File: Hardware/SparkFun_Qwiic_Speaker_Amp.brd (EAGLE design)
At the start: 43.2 x 25.4 mm, 93 parts, among them J1 QWIIC, J2 TRS_INPUT, J6 SCREW, U6 TPA2016D2

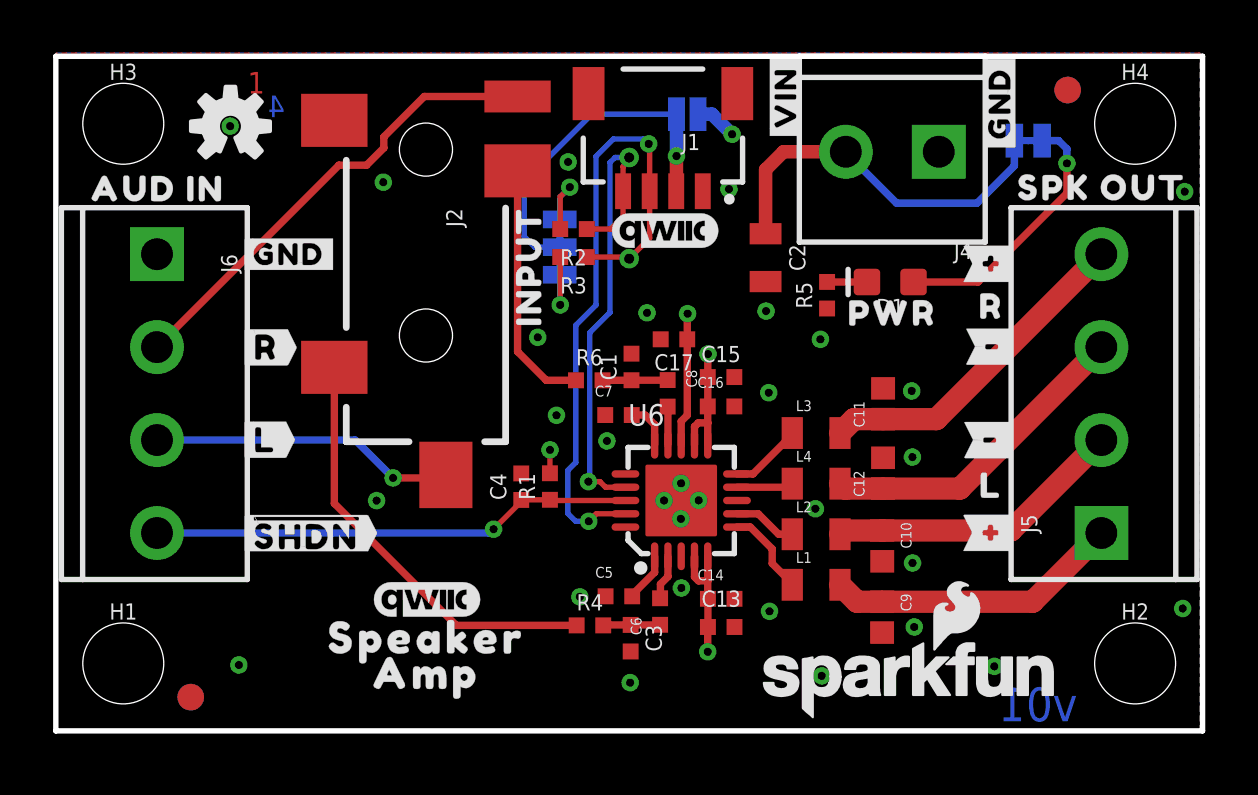
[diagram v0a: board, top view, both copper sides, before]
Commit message: Added more VCC vias for connection to IC power pins.
-also thickened up the VCC traces to IC.
-bumped version to V10 in sch and brd
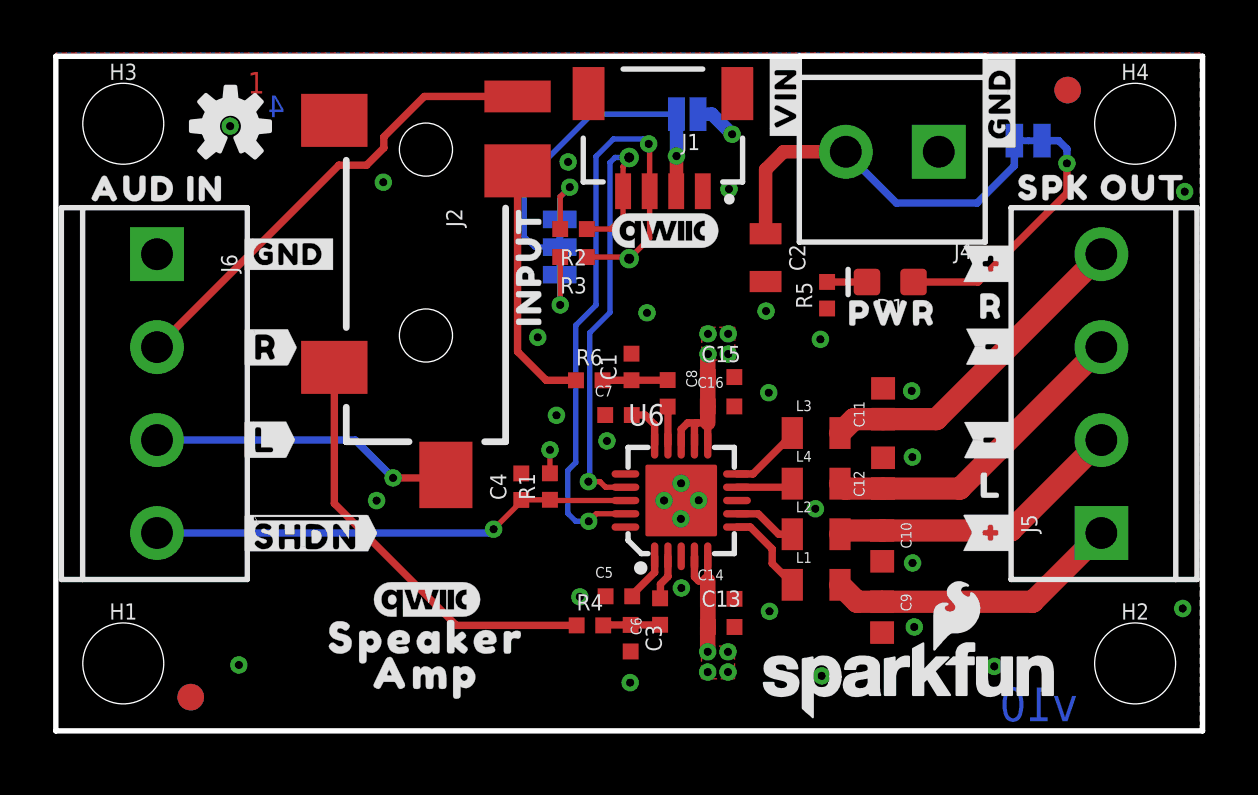
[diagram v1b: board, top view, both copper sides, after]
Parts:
- removed C17: 0.1uF, SparkFun-Capacitors:0402-TIGHT
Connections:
- net GND: no longer C17.2
- net VCC: no longer C17.1
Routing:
- net VCC: track 32.0 -> 28.2 mm, vias 5 -> 10
- added copper zone on layer 1, net VCC
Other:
- board text added: "v10"
- board text removed: "v01"
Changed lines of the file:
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@@
 <drawing>
 <settings>
-<setting alwaysvectorfont="yes"/>
+<setting alwaysvectorfont="no"/>
 <setting verticaltext="up"/>
 </settings>
@@
 <plain>
 <text x="2.54" y="-22.86" size="1.778" layer="51" font="vector">Based on the Lilypad MP3 by Mike Grusin</text>
-<text x="38.464" y="0.363" size="1.27" layer="16" font="vector" ratio="15" rot="SMR0">v01</text>
+<text x="38.464" y="0.363" size="1.27" layer="16" font="vector" ratio="15" rot="SMR0">v10</text>
 <text x="19.05" y="-20.32" size="1.778" layer="51" font="vector">Pete Lewis</text>
 <wire x1="0" y1="0" x2="43.18" y2="0" width="0.2032" layer="20"/>
@@
 <attribute name="VALUE" x="25.04948125" y="12.7603" size="0.6096" layer="27" font="vector" ratio="20" align="top-center"/>
 </element>
-<element name="C17" library="SparkFun-Capacitors" package="0402-TIGHT" value="0.1uF" x="23.276559375" y="14.7447" smashed="yes" rot="R180">
-<attribute name="NAME" x="23.276559375" y="14.1827" size="0.6096" layer="25" font="vector" ratio="20" rot="R180" align="bottom-center"/>
-<attribute name="PROD_ID" value="CAP-16507" x="23.276559375" y="14.7447" size="1.778" layer="27" font="vector" ratio="15" rot="R180" display="off"/>
-<attribute name="VALUE" x="23.276559375" y="15.3067" size="0.6096" layer="27" font="vector" ratio="20" rot="R180" align="top-center"/>
-</element>
 <element name="U$26" library="output" package="#VIN#30" value="" x="29.784040625" y="19.2405" smashed="yes" rot="MR270"/>
 <element name="U$27" library="output" package="#GND#31" value="" x="33.30701875" y="19.065240625" smashed="yes" rot="MR270"/>
@@
 <signal name="GND">
 <contactref element="J1" pad="1"/>
-<polygon width="0.2032" layer="1">
+<polygon width="0.2032" layer="1" rank="2">
 <vertex x="0" y="0"/>
 <vertex x="43.09" y="0"/>
@@
 <contactref element="C15" pad="2"/>
 <via x="26.7436625" y="15.80641875" extent="1-16" drill="0.3048"/>
-<contactref element="C17" pad="2"/>
 <via x="18.85188125" y="11.88211875" extent="1-16" drill="0.3048"/>
 <polygon width="0.2032" layer="2" isolate="0.3048">
@@
 <via x="24.5465625" y="2.976878125" extent="1-16" drill="0.3048"/>
 <wire x1="24.548340625" y1="6.5741" x2="24.548340625" y2="5.648959375" width="0.2794" layer="1"/>
-<wire x1="24.548340625" y1="5.648959375" x2="24.548340625" y2="4.977" width="0.2794" layer="1"/>
+<wire x1="24.548340625" y1="5.648959375" x2="24.548340625" y2="4.977" width="0.5842" layer="1"/>
 <wire x1="24.5545625" y1="4.970778125" x2="24.548340625" y2="4.977" width="0.2794" layer="1"/>
-<wire x1="24.5545625" y1="4.970778125" x2="24.5545625" y2="3.911603125" width="0.2794" layer="1"/>
+<wire x1="24.5545625" y1="4.970778125" x2="24.5545625" y2="3.911603125" width="0.5842" layer="1"/>
 <wire x1="24.554559375" y1="3.9116" x2="24.5545625" y2="3.911603125" width="0.2794" layer="1"/>
 <wire x1="24.554559375" y1="3.9116" x2="24.5465625" y2="3.903603125" width="0.2794" layer="1"/>
-<wire x1="24.5465625" y1="3.903603125" x2="24.5465625" y2="2.976878125" width="0.2794" layer="1"/>
+<wire x1="24.5465625" y1="3.903603125" x2="24.5465625" y2="2.976878125" width="0.5842" layer="1"/>
 <wire x1="24.048340625" y1="6.5741" x2="24.048340625" y2="6.145403125" width="0.2794" layer="1"/>
 <wire x1="24.048340625" y1="6.5741" x2="24.048340625" y2="5.800784375" width="0.2794" layer="1"/>
@@
 <wire x1="24.048340625" y1="5.800784375" x2="24.200165625" y2="5.648959375" width="0.2794" layer="1"/>
 <wire x1="24.548340625" y1="10.7741" x2="24.548340625" y2="11.597640625" width="0.2794" layer="1"/>
-<wire x1="24.548340625" y1="11.597640625" x2="24.548340625" y2="12.2162625" width="0.2794" layer="1"/>
+<wire x1="24.548340625" y1="11.597640625" x2="24.548340625" y2="12.2162625" width="0.5842" layer="1"/>
 <wire x1="24.548340625" y1="12.2162625" x2="24.549478125" y2="12.2174" width="0.2794" layer="1"/>
-<wire x1="24.549478125" y1="12.2174" x2="24.549478125" y2="13.322296875" width="0.2794" layer="1"/>
+<wire x1="24.549478125" y1="12.2174" x2="24.549478125" y2="13.322296875" width="0.5842" layer="1"/>
 <wire x1="24.549478125" y1="13.322296875" x2="24.54948125" y2="13.3223" width="0.2794" layer="1"/>
 <via x="24.556721875" y="14.1884375" extent="1-16" drill="0.3048"/>
-<via x="23.787103125" y="15.709896875" extent="1-16" drill="0.3048"/>
-<contactref element="C17" pad="1"/>
-<wire x1="23.776559375" y1="14.7447" x2="23.776559375" y2="15.699353125" width="0.2794" layer="1"/>
-<wire x1="23.776559375" y1="15.699353125" x2="23.787103125" y2="15.709896875" width="0.2794" layer="1"/>
-<wire x1="23.776559375" y1="11.884278125" x2="23.776559375" y2="14.7447" width="0.2794" layer="1"/>
-<wire x1="24.191340625" y1="11.597640625" x2="24.548340625" y2="11.597640625" width="0.2794" layer="1"/>
 <wire x1="31.65348125" y1="19.872959375" x2="29.7460625" y2="21.780378125" width="0.2794" layer="16"/>
 <wire x1="29.7460625" y1="21.780378125" x2="29.7460625" y2="21.8059" width="0.2794" layer="16"/>
@@
 <wire x1="26.72588125" y1="21.1328" x2="26.72588125" y2="18.718096875" width="0.508" layer="1"/>
 <wire x1="27.39898125" y1="21.8059" x2="26.72588125" y2="21.1328" width="0.508" layer="1"/>
-<wire x1="23.776559375" y1="11.884278125" x2="23.548340625" y2="11.656059375" width="0.2794" layer="1"/>
-<wire x1="23.548340625" y1="11.656059375" x2="23.548340625" y2="10.7741" width="0.2794" layer="1"/>
-<wire x1="24.048340625" y1="10.7741" x2="24.048340625" y2="11.454640625" width="0.2794" layer="1"/>
-<wire x1="24.048340625" y1="11.454640625" x2="24.191340625" y2="11.597640625" width="0.2794" layer="1"/>
-<wire x1="24.54948125" y1="13.3223" x2="24.54948125" y2="14.181196875" width="0.2794" layer="1"/>
+<wire x1="24.54948125" y1="13.3223" x2="24.54948125" y2="14.181196875" width="0.5842" layer="1"/>
 <wire x1="24.54948125" y1="14.181196875" x2="24.556721875" y2="14.1884375" width="0.2794" layer="1"/>
 <contactref element="JP1" pad="2"/>
@@
 <vertex x="43.18" y="0"/>
 </polygon>
-</signal>
+<via x="24.5465625" y="2.214878125" extent="1-16" drill="0.3048"/>
+<via x="25.3085625" y="2.214878125" extent="1-16" drill="0.3048"/>
+<wire x1="23.548340625" y1="11.356340625" x2="23.548340625" y2="10.7741" width="0.2794" layer="1"/>
+<wire x1="24.548340625" y1="11.597640625" x2="24.13" y2="11.597640625" width="0.2794" layer="1"/>
+<wire x1="24.13" y1="11.597640625" x2="23.789640625" y2="11.597640625" width="0.2794" layer="1"/>
+<wire x1="23.789640625" y1="11.597640625" x2="23.548340625" y2="11.356340625" width="0.2794" layer="1"/>
+<wire x1="24.048340625" y1="10.7741" x2="24.048340625" y2="11.51598125" width="0.2794" layer="1"/>
+<wire x1="24.048340625" y1="11.51598125" x2="24.13" y2="11.597640625" width="0.2794" layer="1"/>
+<via x="24.556721875" y="14.9504375" extent="1-16" drill="0.3048"/>
+<via x="25.318721875" y="14.9504375" extent="1-16" drill="0.3048"/>
+<via x="25.3085625" y="2.976878125" extent="1-16" drill="0.3048"/>
+<via x="25.318721875" y="14.1884375" extent="1-16" drill="0.3048"/>
+<polygon width="0.2032" layer="1" isolate="0.3048">
+<vertex x="25.567640625" y="15.196821875"/>
+<vertex x="24.323040625" y="15.196821875"/>
+<vertex x="24.323040625" y="13.964921875"/>
+<vertex x="25.567640625" y="13.964921875"/>
+</polygon>
+<polygon width="0.2032" layer="1" isolate="0.3048">
+<vertex x="25.557478125" y="3.19278125"/>
+<vertex x="24.312878125" y="3.19278125"/>
+<vertex x="24.312878125" y="1.96088125"/>
+<vertex x="25.557478125" y="1.96088125"/>
+</polygon>
+</signal>

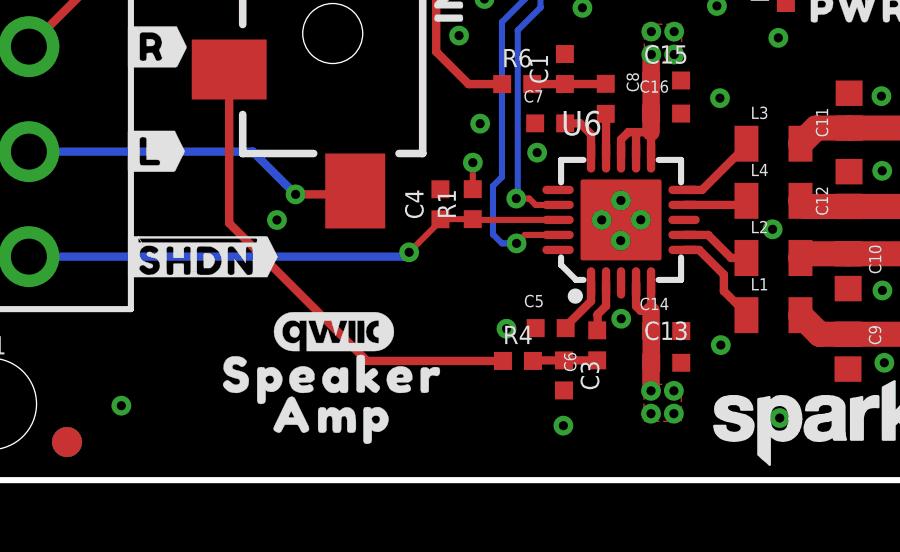
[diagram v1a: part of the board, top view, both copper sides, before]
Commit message: increased qwiic logo size
-fixed one wire stub
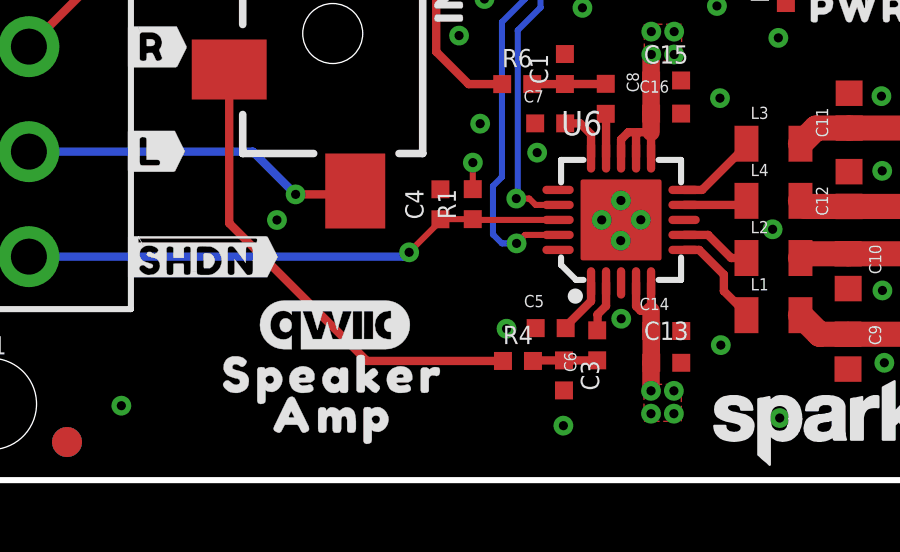
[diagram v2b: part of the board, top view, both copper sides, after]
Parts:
- LOGO1: device SparkFun-Aesthetics:QWIIC_4MM -> SparkFun-Aesthetics:QWIIC_5MM
- moved LOGO1 0.25 mm to (14.0, 5.19)
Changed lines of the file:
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@@
 <setting verticaltext="up"/>
 </settings>
-<grid distance="0.05" unitdist="inch" unit="inch" style="lines" multiple="1" display="yes" altdistance="0.0001" altunitdist="inch" altunit="inch"/>
+<grid distance="0.05" unitdist="inch" unit="inch" style="lines" multiple="1" display="yes" altdistance="0.005" altunitdist="inch" altunit="inch"/>
 <layers>
 <layer number="1" name="Top" color="4" fill="1" visible="yes" active="yes"/>
@@
 <dimension x1="22.86" y1="20.32" x2="0" y2="25.4" x3="11.43" y3="34.29" textsize="1.778" textratio="15" layer="47" dtype="horizontal" unit="inch"/>
 <dimension x1="29.7460625" y1="21.8059" x2="0" y2="25.52" x3="14.87303125" y3="38.1" textsize="1.778" textratio="15" layer="47" dtype="horizontal" unit="inch"/>
-<dimension x1="29.7460625" y1="21.8059" x2="33.2460625" y2="21.8059" x3="31.4960625" y3="30.48" textsize="1.778" textratio="15" layer="47" dtype="horizontal" unit="inch" precision="3"/>
+<dimension x1="29.7460625" y1="21.8059" x2="33.2460625" y2="21.8059" x3="31.4960625" y3="34.29" textsize="1.778" textratio="15" layer="47" dtype="horizontal" unit="inch" precision="3"/>
 <dimension x1="0" y1="25.4" x2="2.54" y2="22.86" x3="-5.08" y3="24.13" textsize="1.778" textratio="15" layer="47" dtype="vertical" unit="inch" precision="3"/>
 <dimension x1="0" y1="0" x2="2.54" y2="2.54" x3="1.27" y3="-3.81" textsize="1.778" textratio="15" layer="47" dtype="horizontal" unit="inch"/>
@@
 <wire x1="30.172659375" y1="21.81351875" x2="30.058359375" y2="21.92781875" width="4.5212" layer="48" style="shortdash"/>
 <wire x1="39.367459375" y1="7.16788125" x2="39.367459375" y2="17.88921875" width="4.5212" layer="48" style="shortdash"/>
+<dimension x1="43.18" y1="25.4" x2="40.64" y2="22.86" x3="41.91" y3="30.48" textsize="1.778" textratio="15" layer="100" dtype="horizontal" unit="inch"/>
+<dimension x1="43.18" y1="25.4" x2="40.64" y2="22.86" x3="54.61" y3="24.13" textsize="1.778" textratio="15" layer="100" dtype="vertical" unit="inch"/>
 </plain>
 <attributes>
@@
 <element name="U$10" library="output" package="###16" value="" x="35.30091875" y="14.4653" smashed="yes"/>
 <element name="U$12" library="output" package="###15" value="" x="35.265359375" y="17.58441875" smashed="yes"/>
-<element name="LOGO1" library="SparkFun-Aesthetics" package="QWIIC_4MM" value="QWIIC_LOGO_4MM" x="13.984" y="4.937521875" smashed="yes"/>
+<element name="LOGO1" library="SparkFun-Aesthetics" package="QWIIC_5MM" value="QWIIC_LOGO_4MM" x="13.984" y="5.191521875" smashed="yes"/>
 <element name="U$14" library="output" package="R21" value="" x="35.2272625" y="15.984221875" smashed="yes"/>
 <element name="U$21" library="output" package="SPK_OUT22" value="" x="39.410640625" y="20.449540625" smashed="yes"/>
@@
 <wire x1="24.554559375" y1="3.9116" x2="24.5465625" y2="3.903603125" width="0.2794" layer="1"/>
 <wire x1="24.5465625" y1="3.903603125" x2="24.5465625" y2="2.976878125" width="0.5842" layer="1"/>
-<wire x1="24.048340625" y1="6.5741" x2="24.048340625" y2="6.145403125" width="0.2794" layer="1"/>
 <wire x1="24.048340625" y1="6.5741" x2="24.048340625" y2="5.800784375" width="0.2794" layer="1"/>
 <wire x1="24.200165625" y1="5.648959375" x2="24.548340625" y2="5.648959375" width="0.2794" layer="1"/>
